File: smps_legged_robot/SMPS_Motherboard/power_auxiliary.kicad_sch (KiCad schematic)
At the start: 5 parts, among them U4 MAX15062A

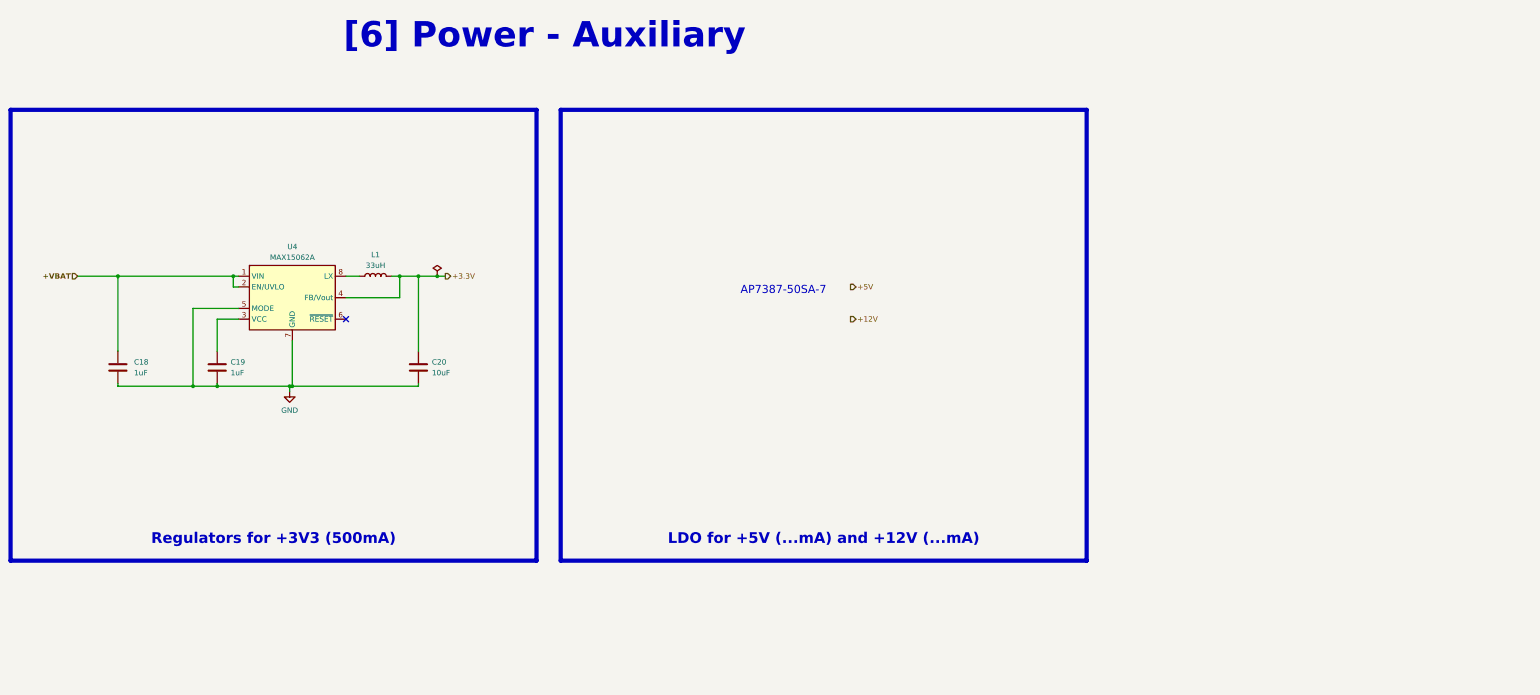
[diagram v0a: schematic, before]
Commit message: Buck module finished pending review
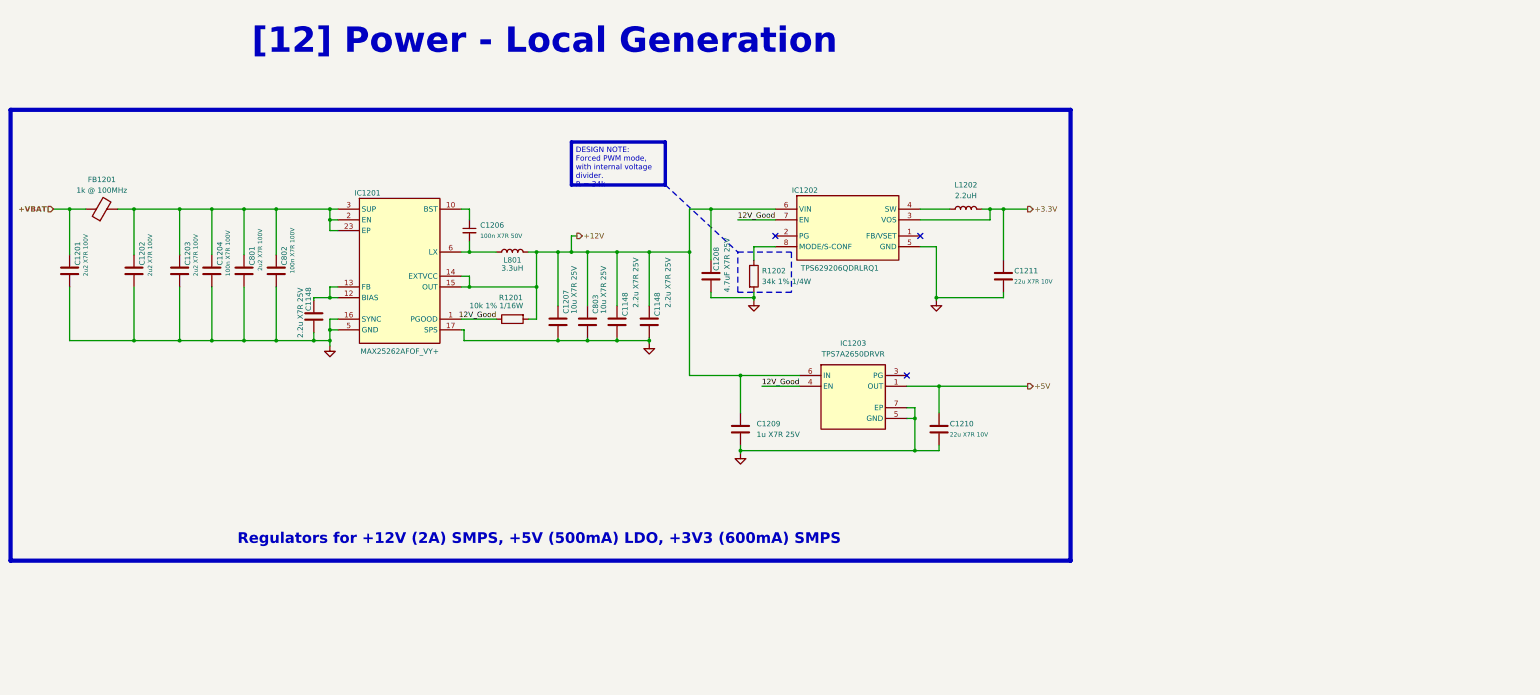
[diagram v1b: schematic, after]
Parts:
- removed C18, C19: 1uF, symbol Device:C
- removed C20: 10uF, symbol Device:C
- removed L1: 33uH, symbol Device:L
- removed U4: MAX15062A, Package_DFN_QFN:DFN-8_2x2mm_P0.5mm, symbol Regulator_Switching:MAX15062A
- added C1148 (x3): 2.2u X7R 25V, 0_capacitor_smd:C_0805_2012_DensityHigh, symbol Device:C
- added C1201, C1202, C1203, C801: 2u2 X7R 100V, 0_capacitor_smd:C_0805_2012_DensityHigh, symbol Device:C
- added C1204, C802: 100n X7R 100V, 0_capacitor_smd:C_0805_2012_DensityHigh, symbol Device:C
- added C1206: 100n X7R 50V, 0_capacitor_smd:C_0402_1005_DensityHigh, symbol Device:C_Small
- added C1207, C803: 10u X7R 25V, 0_capacitor_smd:C_1210_3225_DensityHigh, symbol Device:C
- added C1208: 4.7uF X7R 25V, 0_capacitor_smd:C_1210_3225_DensityHigh, symbol Device:C
- added C1209: 1u X7R 25V, 0_capacitor_smd:C_0603_1608_DensityHigh, symbol Device:C
- added C1210: 22u X7R 10V, 0_capacitor_smd:C_1210_3225_DensityHigh, symbol Device:C
- added C1211: 22u X7R 10V, 0_capacitor_smd:C_0805_2012_DensityHigh, symbol Device:C
- added FB1201: 1k @ 100MHz, 0_resistor_smd:R_0805_2012_DensityHigh, symbol Device:FerriteBead
- added IC1201: MAX25262AFOF_VY+, 0_switching_regulator:MAX25262AFOFVY, symbol MAX25262AFOF_VY+:MAX25262AFOF_VY+
- added IC1202: TPS629206QDRLRQ1, 0_switching_regulator:SOTFL50P160X60-8N, symbol TPS629206QDRLRQ1:TPS629206QDRLRQ1
- added IC1203: TPS7A2650DRVR, 0_switching_regulator:SON65P200X200X80-7N, symbol TPS7A2650DRVR:TPS7A2650DRVR
- added L1202: 2.2uH, 0_switching_regulator:IND_XGL3530_COC, symbol Device:L
- added L801: 3.3uH, 0_switching_regulator:XEL4030682MEC, symbol Device:L
- added R1201: 10k 1% 1/16W, 0_resistor_smd:R_0402_1005_DensityHigh, symbol Device:R
- added R1202: 34k 1% 1/4W, 0_resistor_smd:R_0603_1608_DensityHigh, symbol Device:R
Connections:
- net +12V: now also C1148.2, C1148.2, C1207.2, C1208.2, C1209.2, C803.2, IC1201.14 (EXTVCC), IC1201.15 (OUT), IC1202.6 (VIN), IC1203.6 (IN), L801.2, R1201.2
- net +3.3V: now also C1211.1, IC1202.3 (VOS), L1202.2
- net +5V: now also C1210.1, IC1203.1 (OUT)
- net +VBAT: now also C1201.1, FB1201.1
- net GND: now also C1148.1, C1148.1, C1148.2, C1201.2, C1202.2, C1203.2, C1204.2, C1207.1, C1208.1, C1209.1, C1210.2, C1211.2, C801.2, C802.2, C803.1, IC1201.11 (GND), IC1201.16 (SYNC), IC1201.17 (SPS), IC1201.18 (SPS_2), IC1201.19 (PGND_3), IC1201.21 (PGND_4), IC1201.5 (GND), IC1201.7 (PGND_2), IC1202.5 (GND), IC1203.2 (NC), IC1203.5 (GND), IC1203.7 (EP), R1202.2
- new net: C1206.1, IC1201.10 (BST)
- new net: C1148.1, IC1201.12 (BIAS), IC1201.13 (FB), IC1201.22 (BIAS_2)
- new net: C1202.1, C1203.1, C1204.1, C801.1, C802.1, FB1201.2, IC1201.2 (EN), IC1201.23 (EP), IC1201.3 (SUP), IC1201.9 (SUP_2)
- new net: C1206.2, IC1201.20 (LX_2), IC1201.6 (LX), L801.1
- new net: IC1201.4 (N/C), IC1201.8 (NC)
- new net: IC1202.4 (SW), L1202.1
- new net: IC1202.8 (MODE/S-CONF), R1202.1
- new net 12V_Good: IC1201.1 (PGOOD), IC1202.7 (EN), IC1203.4 (EN), R1201.1
- no-connect marks 1 -> 3
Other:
- note removed: "AP7387-50SA-7"

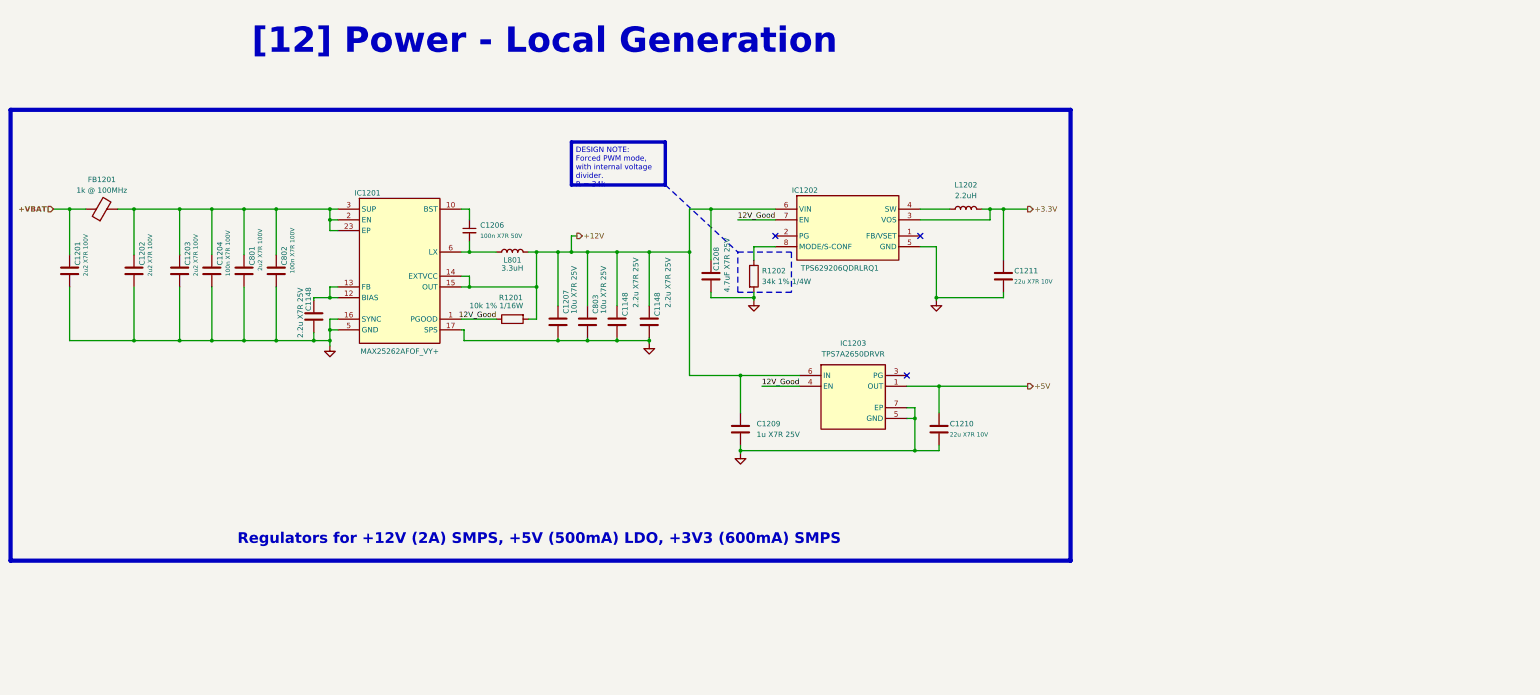
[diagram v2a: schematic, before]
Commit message: Rev 1.0 of smps finished -> waiting for verification
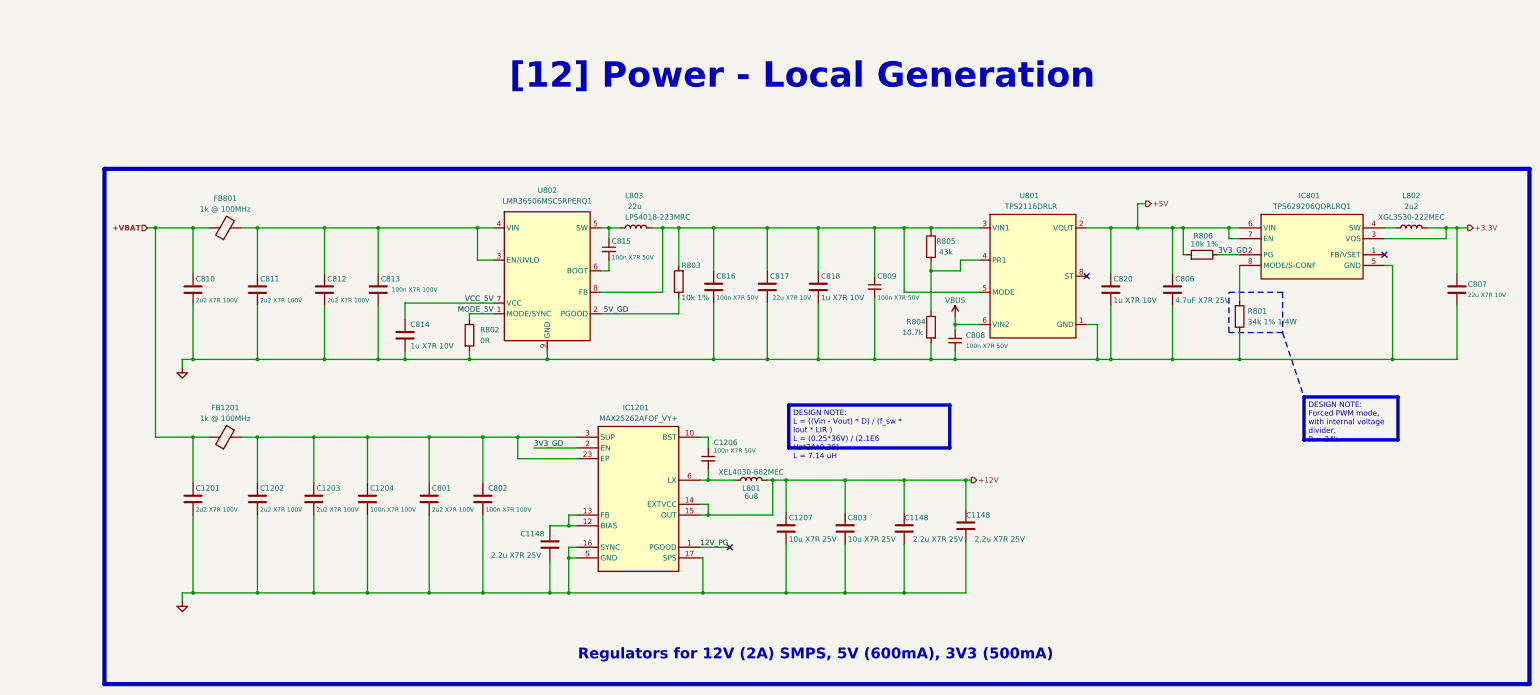
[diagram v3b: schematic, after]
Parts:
- removed C1208: 4.7uF X7R 25V, 0_capacitor_smd:C_1210_3225_DensityHigh, symbol Device:C
- removed C1209: 1u X7R 25V, 0_capacitor_smd:C_0603_1608_DensityHigh, symbol Device:C
- removed C1210: 22u X7R 10V, 0_capacitor_smd:C_1210_3225_DensityHigh, symbol Device:C
- removed C1211: 22u X7R 10V, 0_capacitor_smd:C_0805_2012_DensityHigh, symbol Device:C
- removed IC1202: TPS629206QDRLRQ1, 0_switching_regulator:SOTFL50P160X60-8N, symbol TPS629206QDRLRQ1:TPS629206QDRLRQ1
- removed IC1203: TPS7A2650DRVR, 0_switching_regulator:SON65P200X200X80-7N, symbol TPS7A2650DRVR:TPS7A2650DRVR
- removed L1202: 2.2uH, 0_switching_regulator:IND_XGL3530_COC, symbol Device:L
- removed R1201: 10k 1% 1/16W, 0_resistor_smd:R_0402_1005_DensityHigh, symbol Device:R
- removed R1202: 34k 1% 1/4W, 0_resistor_smd:R_0603_1608_DensityHigh, symbol Device:R
- added C806: 4.7uF X7R 25V, 0_capacitor_smd:C_1210_3225_DensityHigh, symbol Device:C
- added C807: 22u X7R 10V, 0_capacitor_smd:C_0805_2012_DensityHigh, symbol Device:C
- added C808, C809, C815: 100n X7R 50V, 0_capacitor_smd:C_0402_1005_DensityHigh, symbol Device:C_Small
- added C810, C811: 2u2 X7R 100V, 0_capacitor_smd:C_0805_2012_DensityHigh, symbol Device:C
- added C812: 2u2 X7R 100V, 0_resistor_smd:R_0805_2012_DensityHigh, symbol Device:C
- added C813: 100n X7R 100V, 0_capacitor_smd:C_0603_1608_DensityHigh, symbol Device:C
- added C814, C818, C820: 1u X7R 10V, 0_capacitor_smd:C_0402_1005_DensityHigh, symbol Device:C
- added C816: 100n X7R 50V, 0_capacitor_smd:C_0402_1005_DensityHigh, symbol Device:C
- added C817: 22u X7R 10V, 0_capacitor_smd:C_0805_2012_DensityHighest, symbol Device:C
- added FB801: 1k @ 100MHz, 0_resistor_smd:R_0805_2012_DensityHigh, symbol Device:FerriteBead
- added IC801: TPS629206QDRLRQ1, 0_switching_regulator:SOTFL50P160X60-8N, symbol TPS629206QDRLRQ1:TPS629206QDRLRQ1
- added L802: 2u2, 0_switching_regulator:IND_XGL3530_COC, symbol Device:L
- added L803: 22u, 0_inductor_smd:L_Coilcraft_LPS4018, symbol Device:L
- added R801: 34k 1% 1/4W, 0_resistor_smd:R_0603_1608_DensityHigh, symbol Device:R
- added R802: 0R, 0_resistor_smd:R_0402_1005_DensityHigh, symbol Device:R
- added R803, R806: 10k 1%, 0_resistor_smd:R_0402_1005_DensityHigh, symbol Device:R
- added R804: 10.7k, 0_resistor_smd:R_0402_1005_DensityHigh, symbol Device:R
- added R805: 43k, 0_resistor_smd:R_0402_1005_DensityHigh, symbol Device:R
- added U801: TPS2116DRLR, 0_switching_regulator:SOTFL50P160X60-8N, symbol 0_mux:TPS2116DRLR
- added U802: LMR36506MSC5RPERQ1, 0_switching_regulator:LMR36503, symbol 0_switching_regulator:LMR36506MSC5RPERQ1
- L801: value 3.3uH -> 6u8; footprint 0_switching_regulator:XEL4030682MEC -> 0_inductor_smd:XEL4030682MEC
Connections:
- net +3.3V: now also C807.1, IC801.3 (VOS), L802.2
- net +5V: now also C806.2, C820.1, IC801.6 (VIN), IC801.7 (EN), R806.2, U801.2 (VOUT), U801.7 (VOUT)
- net +VBAT: now also C810.1, FB801.1
- net GND: now also C806.1, C807.2, C808.2, C809.2, C810.2, C811.2, C812.2, C813.2, C814.2, C816.2, C817.2, C818.2, C820.2, IC801.5 (GND), R801.2, R802.2, R804.2, U801.1 (GND), U802.9 (GND)
- net at C1202.1, C1203.1, C1204.1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: no longer IC1201.2 (EN)
- net 12V_Good renamed 12V_PG
- new net: C809.1, C816.1, C817.1, C818.1, L803.2, R803.2, R805.1, U801.3 (VIN1), U801.5 (MODE), U802.8 (FB)
- new net: C811.1, C812.1, C813.1, FB801.2, U802.3 (EN/UVLO), U802.4 (VIN)
- new net: C815.1, L803.1, U802.5 (SW)
- new net: C815.2, U802.6 (BOOT)
- new net: R804.1, R805.2, U801.4 (PR1)
- new net: IC801.4 (SW), L802.1
- new net: IC801.8 (MODE/S-CONF), R801.1
- new net 3V3_GD: IC1201.2 (EN), IC801.2 (PG), R806.1
- new net 5V_GD: R803.1, U802.2 (PGOOD)
- new net MODE_5V: R802.1, U802.1 (MODE/SYNC)
- new net VBUS: C808.1, U801.6 (VIN2)
- new net VCC_5V: C814.1, U802.7 (VCC)
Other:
- moved on the sheet: C1148, C1201, C1202, C1203, C1204, C1206, C1207, C801, C802, C803, FB1201, IC1201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

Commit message: Little change, ready to order
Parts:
- removed L802: 2u2, 0_switching_regulator:IND_XGL3530_COC, symbol Device:L
- added L3: 2u2, 0_inductor_smd:L_Coilcraft_LPS3314, symbol Device:L
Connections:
- net +3.3V: now also L3.2
- net at IC801.4 (SW): now also L3.1
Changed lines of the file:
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@@
+    )
+  )
+  (symbol (lib_id "Device:L") (at 353.695 67.945 90) (unit 1)
+    (in_bom yes) (on_board yes) (dnp no)
+    (property "Reference" "L3" (at 351.155 60.325 90)
+      (effects (font (size 1.27 1.27)) (justify right))
+    )
+    (property "Value" "2u2" (at 351.155 62.865 90)
+      (effects (font (size 1.27 1.27)) (justify right))
+    )
+    (property "Footprint" "0_inductor_smd:L_Coilcraft_LPS3314" (at 353.695 67.945 0)
+      (effects (font (size 1.27 1.27)) hide)
+    )
+    (property "Datasheet" "https://www.coilcraft.com/getmedia/3ba581dc-6d87-4be6-9dea-9167ac97554d/lps3314.pdf" (at 353.695 67.945 0)
+      (effects (font (size 1.27 1.27)) hide)
+    )
+    (property "Manufacturer Part Number" "LPS3314-222MRC" (at 344.805 65.405 90)
+      (effects (font (size 1.27 1.27)) (justify right))
+    )
+    (property "Supplier 1" "Mouser" (at 353.695 67.945 90)
+      (effects (font (size 1.27 1.27)) hide)
+    )
+    (property "Supplier Part Number 1" "994-LPS3314-222MRC" (at 353.695 67.945 90)
+      (effects (font (size 1.27 1.27)) hide)
+    )
+    (property "Description" "Power Inductors - SMD 2.2uH Shld 20% 1.2A 100 mOhms" (at 353.695 67.945 0)
+      (effects (font (size 1.27 1.27)) hide)
+    )
+    (property "Manufacturer" "Coilcraft" (at 353.695 67.945 0)
+      (effects (font (size 1.27 1.27)) hide)
+    )
+    (pin "1")
+    (pin "2")
+    (instances
+      (project "smps_legged_robot"
+        (path "/0650c7a8-acba-429c-9f8e-eec0baf0bc1c/fede4c36-00cc-4d3d-b71c-5243ba232202/90980504-ca7e-4d0f-ada1-af3b0bda141f"
+          (reference "L802") (unit 1)
+        )
+      )
     )
   )
@@
         )
       )
-    )
-  )
-  (symbol (lib_id "Device:L") (at 353.695 67.945 90) (unit 1)
-    (in_bom yes) (on_board yes) (dnp no)
-    (property "Reference" "L802" (at 353.695 60.325 90)
-      (effects (font (size 1.27 1.27)))
-    )
-    (property "Value" "2u2" (at 353.695 62.865 90)
-      (effects (font (size 1.27 1.27)))
-    )
-    (property "Footprint" "0_switching_regulator:IND_XGL3530_COC" (at 353.695 67.945 0)
-      (effects (font (size 1.27 1.27)) hide)
-    )
-    (property "Datasheet" "XGL3530-222MEC" (at 353.695 65.405 90)
-      (effects (font (size 1.27 1.27)))
-    )
-    (pin "1")
-    (pin "2")
-    (instances
-      (project "smps_legged_robot"
-        (path "/0650c7a8-acba-429c-9f8e-eec0baf0bc1c/fede4c36-00cc-4d3d-b71c-5243ba232202/90980504-ca7e-4d0f-ada1-af3b0bda141f"
-          (reference "L802") (unit 1)
-        )
-      )

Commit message: Geode test board ready to order
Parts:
- added D801, D802: GREEN, LED_SMD:LED_0603_1608Metric, symbol Device:LED
- added Q1801 (x2): PMV90ENER, 0_package_SOT_TO_SMD:SOT-23-3, symbol Simulation_SPICE:NMOS
- added R807, R808: 470R 1% 1/8W, 0_resistor_smd:R_0402_1005_DensityHigh, symbol Device:R
- R805: value 43k -> 37k
- renumbered L3 to L802
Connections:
- net +12V: now also R807.1, R808.1
- net 3V3_GD: now also Q1801.1 (G)
- net 5V_GD: now also Q1801.1 (G)
- net GND: now also Q1801.2 (S), Q1801.2 (S)
- new net: D801.1 (K), Q1801.3 (D)
- new net: D801.2 (A), R807.2
- new net: D802.1 (K), Q1801.3 (D)
- new net: D802.2 (A), R808.2
